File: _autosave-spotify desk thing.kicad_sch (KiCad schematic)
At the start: 25 parts, among them J1 AudioJack3_Ground, J3 USB_C_Receptacle_USB2.0_16P, SW1 RESET, SW2 BOOT, U1 ESP32-S3-WROOM-1-N4, U2 PCM5242RHBR, U3 EC11E18244A5, U9 USBLC6-2SC6

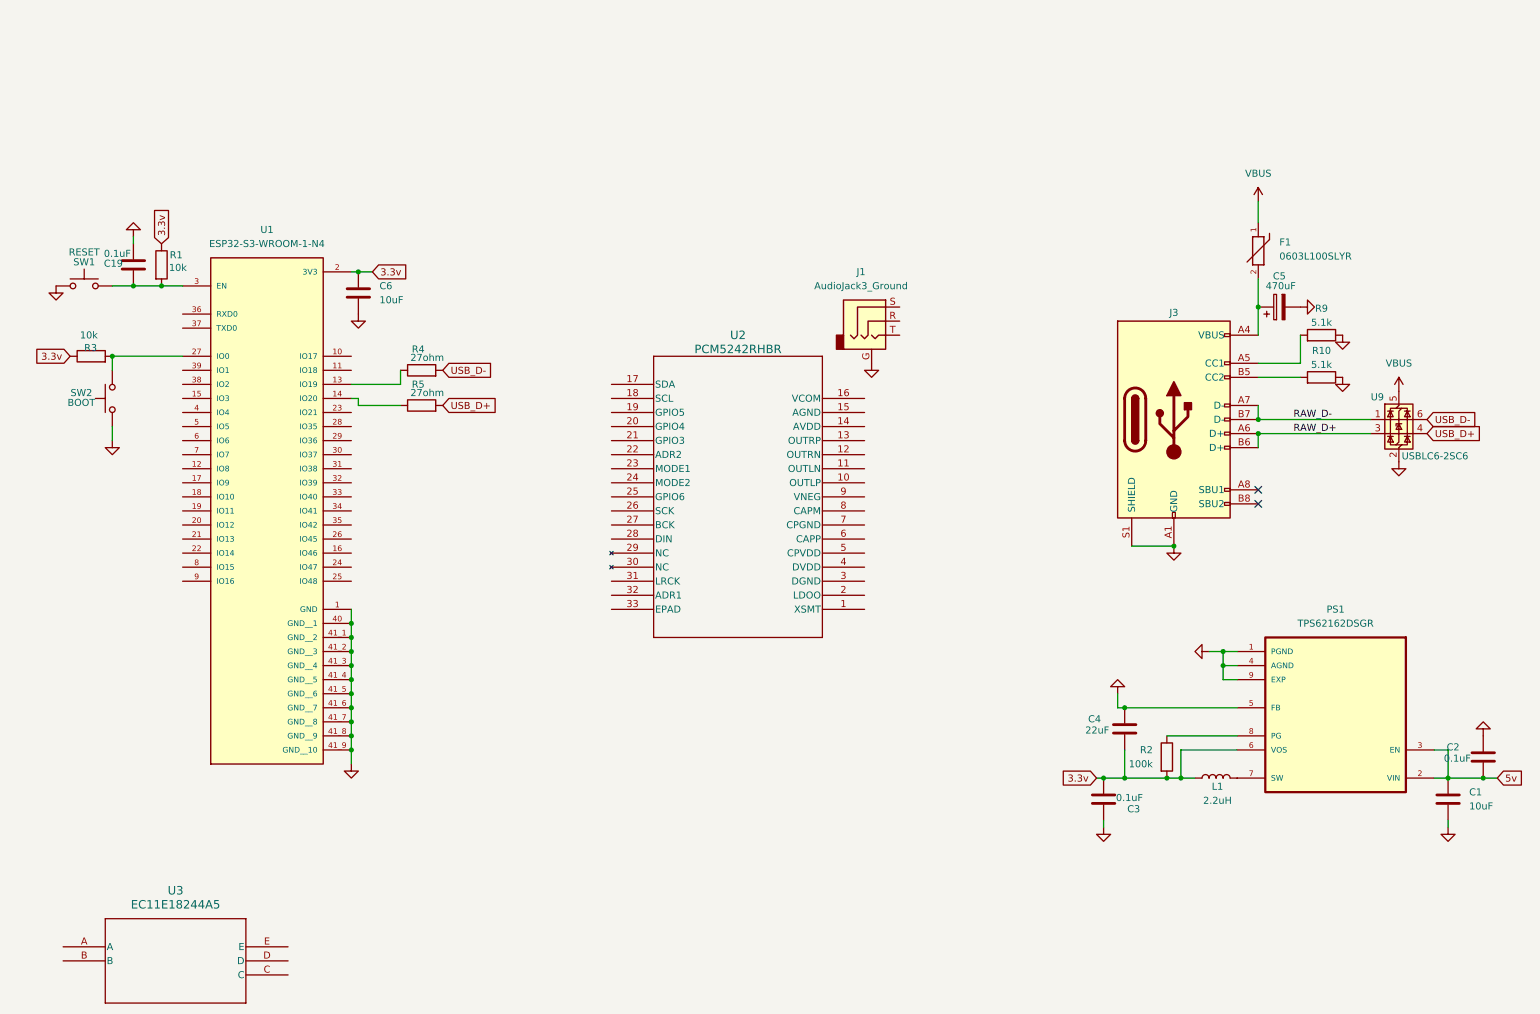
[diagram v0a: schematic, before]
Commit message: fixed wiring and wired up AMP
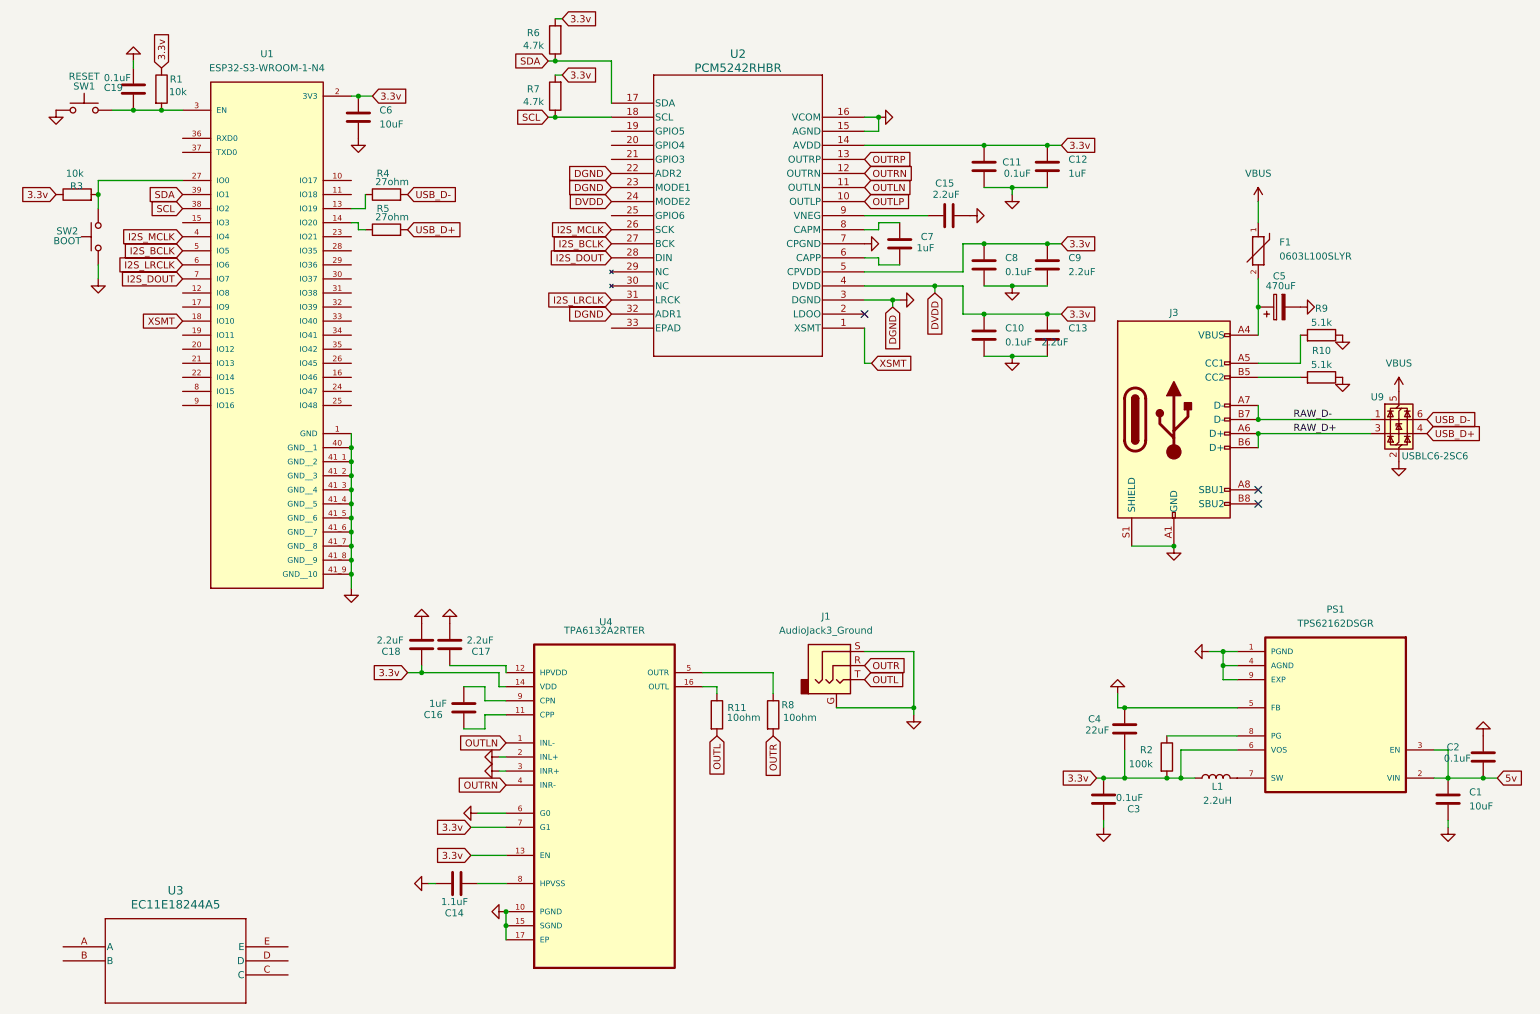
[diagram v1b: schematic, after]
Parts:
- added C10, C11, C8: 0.1uF, Capacitor_SMD:C_0402_1005Metric, symbol Device:C
- added C12, C16, C7: 1uF, Capacitor_SMD:C_0402_1005Metric, symbol Device:C
- added C13, C15, C17, C18, C9: 2.2uF, Capacitor_SMD:C_0402_1005Metric, symbol Device:C
- added C14: 1.1uF, Capacitor_SMD:C_0402_1005Metric, symbol Device:C
- added R11, R8: 10ohm, Resistor_SMD:R_0603_1608Metric, symbol Device:R
- added R6, R7: 4.7k, Resistor_SMD:R_0603_1608Metric, symbol Device:R
- added U4: TPA6132A2RTER, TPA6132A2RTER:QFN50P300X300X80-16N, symbol TPA6132A2RTER:TPA6132A2RTER
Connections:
- net 3.3v: now also U2.14 (AVDD), U2.24 (MODE2), U2.4 (DVDD), U2.5 (CPVDD), C10.1, C11.1, C12.1, C13.1, C18.1, C8.1, C9.1, R6.2, R7.2, U4.13 (EN), U4.14 (VDD), U4.7 (G1)
- net GND: now also J1.S, U2.15 (AGND), U2.16 (VCOM), U2.22 (ADR2), U2.23 (MODE1), U2.3 (DGND), U2.32 (ADR1), U2.7 (CPGND), C10.2, C11.2, C12.2, C13.2, C14.1, C15.2, C17.2, C18.2, C8.2, C9.2, U4.10 (PGND), U4.15 (SGND), U4.17 (EP), U4.2 (INL+), U4.3 (INR+), U4.6 (G0)
- net XSMT: now reaches U2.1 (XSMT)
- net XSMT: now also U1.18 (IO10)
- net OUTLP: now reaches U2.10 (OUTLP)
- net OUTLN: now reaches U2.11 (OUTLN)
- net OUTLN: now also U4.1 (INL-)
- net OUTRN: now reaches U2.12 (OUTRN)
- net OUTRN: now also U4.4 (INR-)
- net OUTRP: now reaches U2.13 (OUTRP)
- net SDA: now reaches U2.17 (SDA)
- net SDA: now also U1.39 (IO1), R6.1
- net SCL: now reaches U2.18 (SCL)
- net SCL: now also U1.38 (IO2), R7.1
- net I2S_MCLK: now reaches U2.26 (SCK)
- net I2S_MCLK: now also U1.4 (IO4)
- net I2S_BCLK: now reaches U2.27 (BCK)
- net I2S_BCLK: now also U1.5 (IO5)
- net I2S_DOUT: now reaches U2.28 (DIN)
- net I2S_DOUT: now also U1.7 (IO7)
- net I2S_LRCLK: now reaches U2.31 (LRCK)
- net I2S_LRCLK: now also U1.6 (IO6)
- net at U2.6 (CAPP): now also C7.2
- net at U2.8 (CAPM): now also C7.1
- net at U2.9 (VNEG): now also C15.1
- net OUTR: now reaches J1.R
- net OUTR: now also R8.2
- net OUTL: now reaches J1.T
- net OUTL: now also R11.2
- new net: R11.1, U4.16 (OUTL)
- new net: R8.1, U4.5 (OUTR)
- new net: C16.1, U4.11 (CPP)
- new net: C16.2, U4.9 (CPN)
- new net: C14.2, U4.8 (HPVSS)
- new net: C17.1, U4.12 (HPVDD)
- no-connect marks 2 -> 3
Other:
- moved on the sheet: C19, C6, J1, R1, R3, R4, R5, SW1, SW2, U1, U2
